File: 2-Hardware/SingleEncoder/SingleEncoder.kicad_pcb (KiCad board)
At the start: 2 copper layers, 20.3 x 57.2 mm, 26 parts, among them J1 PMOD_SINGLE, P1 CONN_01X06, Q1 MMBT2222, Q2 MMBT2222, U1 TPS60131, U2 MCP6L02, U3 ILD213T

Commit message: Finalized BOM
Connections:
- U3 pad 1: Net-(R3-Pad1) -> Net-(R4-Pad1)
- U3 pad 3: Net-(R4-Pad1) -> Net-(R3-Pad1)
- U3 pad 6: Net-(Q2-PadB) -> Net-(Q1-PadB)
- U3 pad 8: Net-(Q1-PadB) -> Net-(Q2-PadB)
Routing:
- net /ENC_A: track 0.13 -> 24.7 mm, vias 0 -> 2
- net GND: track 23.8 -> 41.8 mm, vias 5 -> 6
- net +5V: track 33.9 -> 51.8 mm, vias 0 -> 1
- net VCC: track 64.6 -> 67.8 mm
- net Net-(Q2-PadB): track 4.28 -> 7.20 mm
- net Net-(Q1-PadB): track 12.1 -> 9.22 mm
- net Net-(R4-Pad1): track 1.70 -> 2.72 mm
- net Net-(R3-Pad1): track 3.75 -> 2.72 mm
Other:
- net class Default: via_dia 0.6 -> 0.635; via_drill 0.4 -> 0.381
- board text added: "A"
- board text added: "B"
- board text added: "GND"
- board text added: "Quadrature Encoder PMOD-Compatible Interface"
- board text added: "Revision A Designed by: Ian McInerney"

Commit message: Added 4-pin connector behind the DIN connector
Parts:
- added P2: CONN_01X04, Connectors:CONN_2.54mm_1x4, F.Cu at (126.2, 107.6)
- moved D1 11.7 mm to (133.5, 95.9), turned to 180 degrees
- moved R2 9.56 mm to (133.5, 101.3), turned to 180 degrees
- moved C7 6.59 mm to (120.7, 101.3), turned to 0 degrees
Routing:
- net /ENC_A: track 24.7 -> 37.7 mm
- net /ENC_B: track 11.6 -> 20.3 mm
- net +5V: track 51.8 -> 54.0 mm
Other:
- board text added: "+5"

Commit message: Associated footprints, reimported to board. Layout not done.
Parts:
- removed Q1, Q2: MMBT2222, Transistors:TRANS_SOT-23-3_BEC
- removed R5, R6, R7, R8: 10k, SMD:SMD_0805
- removed U2: MCP6L02, SMD:SSOP_08_3.0mm_3.0mm_0.65mm
- removed U3: ILD213T, SMD:SOIC_08_4.0mm_5.8mm_1.27mm
- added AT1: TXB0102, SMD:SSOP_08_3.0mm_2.0mm_0.5mm, F.Cu at (151.1, 72.6)
- added C8: CAP, SMD:SMD_0805, F.Cu at (150.9, 79.1)
- added D2: PLVA653A, Diodes:DIODE_SOT-23-3, F.Cu at (157.4, 72.3)
- added D3: PLVA653A, Diodes:DIODE_SOT-23-3, F.Cu at (164.1, 72.3)
- C7: value 0.1uF -> CAP
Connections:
- net /PWR_EN renamed /EN
- C7 pad 1: GND -> VCC
- C7 pad 2: +5V -> GND
- R3 pad 2: Net-(R3-Pad2) -> /ENC_A
- R4 pad 2: Net-(R4-Pad2) -> /ENC_B
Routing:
- net (no net): track 0.00 -> 39.3 mm, vias 0 -> 4
- net GND: track 41.6 -> 25.6 mm, vias 6 -> 1
- net Net-(Q1-PadB): track 9.22 -> 0.00 mm
- net +5V: track 54.0 -> 45.6 mm
- net /ENC_A: track 37.7 -> 45.3 mm
- net Net-(R3-Pad2): track 7.60 -> 0.00 mm
- net Net-(Q2-PadB): track 7.20 -> 0.00 mm
- net /ENC_B: track 20.3 -> 27.5 mm
- net Net-(R4-Pad2): track 7.18 -> 0.00 mm
- net VCC: track 67.8 -> 69.4 mm, vias 1 -> 2

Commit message: Updated board layout to use level shifter
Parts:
- C7, C8: value CAP -> 0.1uF
- R1: moved to F.Cu
- moved D3 45.7 mm to (123.6, 93.3), turned to 90 degrees
- moved D2 35.4 mm to (128.9, 93.3), turned to 270 degrees
- moved C8 31.2 mm to (120.7, 86.7), turned to 180 degrees
- moved AT1 28.6 mm to (126.3, 86.7), turned to 90 degrees
- moved C7 18.6 mm to (132.0, 86.6)
- moved TP3 8.41 mm to (126.2, 79.4)
- moved R1 8.15 mm to (126.2, 82.8)
- moved R3 1.40 mm to (127.5, 99.1)
- moved R4 1.40 mm to (125.0, 99.1)
- moved TP1 1.27 mm to (133.9, 79.4)
- moved TP2 1.27 mm to (118.6, 79.4)
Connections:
- AT1 pad 2: Net-(AT1-Pad2) -> GND
- AT1 pad 3: Net-(AT1-Pad3) -> VCC
- AT1 pad 4: Net-(AT1-Pad4) -> /LOGIC_A
- AT1 pad 6: Net-(AT1-Pad6) -> /EN
- AT1 pad 7: Net-(AT1-Pad7) -> +5V
- D2 pad C: Net-(D2-PadC) -> Net-(AT1-Pad1)
- J1 pad 2: /LOGIC_B -> Net-(J1-Pad2)
- J1 pad 4: Net-(J1-Pad4) -> /LOGIC_B
- R3 pad 1: Net-(D2-PadC) -> Net-(AT1-Pad1)
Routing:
- net (no net): track 39.3 -> 0.00 mm, vias 4 -> 0
- net /ENC_A: track 45.3 -> 19.6 mm, vias 2 -> 0
- net /ENC_B: track 27.5 -> 14.1 mm
- net Net-(AT1-Pad1): track 0.00 -> 10.9 mm
- net Net-(AT1-Pad8): track 2.72 -> 10.8 mm
- net GND: track 25.6 -> 17.9 mm, vias 1 -> 5
- net +5V: track 45.6 -> 52.5 mm, vias 1 -> 2
- net /EN: track 44.5 -> 38.1 mm
- net VCC: track 69.4 -> 64.4 mm, vias 2 -> 1
- net /LOGIC_A: track 12.6 -> 16.0 mm
- net Net-(D2-PadC): track 2.72 -> 0.00 mm
- net /LOGIC_B: track 18.8 -> 20.9 mm
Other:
- net class EN added: clearance 0.2, trace_width 0.1524, via_dia 0.635, via_drill 0.381
- rule trace_min: 0.2 -> 0.1524
- board text added: "Revision B Designed by: Ian McInerney"
- board text removed: "Revision A Designed by: Ian McInerney"

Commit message: Updated PMOD connector holes
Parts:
- J1: footprint Connectors:PMOD_SINGLE_MALE -> Digilent:PMOD_SINGLE_MALE
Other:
- rule pad_to_mask_clearance: 0 -> 0.0762
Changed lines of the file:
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@@
     (links 60)
     (no_connects 0)
-    (area 116.027999 68.656999 136.448001 125.907001)
+    (area 114.179905 68.431999 138.296096 127.765)
     (thickness 1.6)
     (drawings 13)
@@
     (pad_size 3.38 2.4)
     (pad_drill 0)
-    (pad_to_mask_clearance 0)
+    (pad_to_mask_clearance 0.0762)
+    (solder_mask_min_width 0.1016)
     (aux_axis_origin 0 0)
     (visible_elements FFFFFF7F)
@@
     )
   )
-  (module Connectors:PMOD_SINGLE_MALE locked (layer F.Cu)
-    (at 126.238 70.485)
-    (fp_text reference J1 (at 5.588 4.318) (layer F.SilkS)
-      (effects (font (size 1 1) (thickness 0.15)))
-    )
-    (fp_text value PMOD_SINGLE (at 0 0) (layer F.Fab) hide
-      (effects (font (size 1 1) (thickness 0.15)))
-    )
-    (fp_line (start -10.16 -1.778) (end 10.16 -1.778) (layer Dwgs.User) (width 0.15))
-    (fp_line (start 5.08 0.762) (end 5.08 3.302) (layer F.SilkS) (width 0.15))
-    (fp_line (start 7.62 0.762) (end 7.62 3.302) (layer F.SilkS) (width 0.15))
-    (fp_line (start 7.62 3.302) (end -7.62 3.302) (layer F.SilkS) (width 0.15))
-    (fp_line (start -7.62 3.302) (end -7.62 0.762) (layer F.SilkS) (width 0.15))
-    (fp_line (start -7.62 0.762) (end 7.62 0.762) (layer F.SilkS) (width 0.15))
-    (pad 1 thru_hole rect (at 6.35 2.032 180) (size 1.524 1.524) (drill 0.762) (layers *.Cu *.Mask F.SilkS)
-      (net 7 /LOGIC_A))
-    (pad 2 thru_hole circle (at 3.81 2.032 180) (size 1.524 1.524) (drill 0.762) (layers *.Cu *.Mask F.SilkS)
-      (net 19 "Net-(J1-Pad2)"))
-    (pad 3 thru_hole circle (at 1.27 2.032 180) (size 1.524 1.524) (drill 0.762) (layers *.Cu *.Mask F.SilkS)
-      (net 16 /EN))
-    (pad 4 thru_hole circle (at -1.27 2.032 180) (size 1.524 1.524) (drill 0.762) (layers *.Cu *.Mask F.SilkS)
-      (net 8 /LOGIC_B))
-    (pad 5 thru_hole circle (at -3.81 2.032 180) (size 1.524 1.524) (drill 0.762) (layers *.Cu *.Mask F.SilkS)
-      (net 2 GND))
-    (pad 6 thru_hole circle (at -6.35 2.032 180) (size 1.524 1.524) (drill 0.762) (layers *.Cu *.Mask F.SilkS)
-      (net 1 VCC))
-    (model 3D/Connectors/CONN_1x6_Male.wrl
-      (at (xyz -0.3 0.31 0.096))
-      (scale (xyz 0.3937 0.3937 0.3937))
-      (rotate (xyz 0 180 180))
-    )
-  )
   (module SMD:SMD_0805 (layer F.Cu)
     (at 126.238 82.804 270)
@@
       (scale (xyz 0.3937 0.3937 0.3937))
       (rotate (xyz 0 0 90))
+    )
+  )
+  (module Digilent:PMOD_SINGLE_MALE locked (layer F.Cu)
+    (at 126.238 70.485)
+    (fp_text reference J1 (at 5.588 4.318) (layer F.SilkS)
+      (effects (font (size 1 1) (thickness 0.15)))
+    )
+    (fp_text value PMOD_SINGLE (at 0 0) (layer F.Fab) hide
+      (effects (font (size 1 1) (thickness 0.15)))
+    )
+    (fp_line (start -10.16 -1.778) (end 10.16 -1.778) (layer Dwgs.User) (width 0.15))
+    (fp_line (start 5.08 0.762) (end 5.08 3.302) (layer F.SilkS) (width 0.15))
+    (fp_line (start 7.62 0.762) (end 7.62 3.302) (layer F.SilkS) (width 0.15))
+    (fp_line (start 7.62 3.302) (end -7.62 3.302) (layer F.SilkS) (width 0.15))
+    (fp_line (start -7.62 3.302) (end -7.62 0.762) (layer F.SilkS) (width 0.15))
+    (fp_line (start -7.62 0.762) (end 7.62 0.762) (layer F.SilkS) (width 0.15))
+    (pad 1 thru_hole rect (at 6.35 2.032 180) (size 1.7018 1.7018) (drill 0.9906) (layers *.Cu *.Mask F.SilkS)
+      (net 7 /LOGIC_A))
+    (pad 2 thru_hole circle (at 3.81 2.032 180) (size 1.778 1.778) (drill 0.9906) (layers *.Cu *.Mask F.SilkS)
+      (net 19 "Net-(J1-Pad2)"))
+    (pad 3 thru_hole circle (at 1.27 2.032 180) (size 1.778 1.778) (drill 0.9906) (layers *.Cu *.Mask F.SilkS)
+      (net 16 /EN))
+    (pad 4 thru_hole circle (at -1.27 2.032 180) (size 1.778 1.778) (drill 0.9906) (layers *.Cu *.Mask F.SilkS)
+      (net 8 /LOGIC_B))
+    (pad 5 thru_hole circle (at -3.81 2.032 180) (size 1.778 1.778) (drill 0.9906) (layers *.Cu *.Mask F.SilkS)
+      (net 2 GND))
+    (pad 6 thru_hole circle (at -6.35 2.032 180) (size 1.778 1.778) (drill 0.9906) (layers *.Cu *.Mask F.SilkS)
+      (net 1 VCC))
+    (model 3D/Connectors/CONN_1x6_Male.wrl
+      (at (xyz -0.3 0.31 0.096))
+      (scale (xyz 0.3937 0.3937 0.3937))
+      (rotate (xyz 0 180 180))
     )
   )
@@
   (segment (start 129.0265 85.991) (end 129.0265 84.2065) (width 0.25) (layer F.Cu) (net 7))
   (segment (start 129.0265 84.2065) (end 133.858 79.375) (width 0.25) (layer F.Cu) (net 7))
-  (segment (start 118.618 79.375) (end 122.4915 79.375) (width 0.25) (layer F.Cu) (net 8) (status 400000))
-  (segment (start 123.698 73.787) (end 124.968 72.517) (width 0.25) (layer F.Cu) (net 8) (status 800000))
+  (segment (start 118.618 79.375) (end 122.4915 79.375) (width 0.25) (layer F.Cu) (net 8))
+  (segment (start 123.698 73.787) (end 124.968 72.517) (width 0.25) (layer F.Cu) (net 8))
   (segment (start 123.698 78.1685) (end 123.698 73.787) (width 0.25) (layer F.Cu) (net 8))
   (segment (start 122.4915 79.375) (end 123.698 78.1685) (width 0.25) (layer F.Cu) (net 8))

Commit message: Updated isolation circuit
- Swapped TXB0102 for 2 TXB0101
- Re-did board layout to accomodate new parts
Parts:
- added AT2: TXB0101, SMD:SOT-23-6, F.Cu at (121.9, 86.2)
- added C10: 0.1uF, SMD:SMD_0805, F.Cu at (118.7, 86.2)
- added C9: 0.1uF, SMD:SMD_0805, F.Cu at (125.2, 86.3)
- AT1: value TXB0102 -> TXB0101; footprint SMD:SSOP_08_3.0mm_2.0mm_0.5mm -> SMD:SOT-23-6
- moved C8 6.68 mm to (127.3, 86.3), turned to 0 degrees
- moved AT1 4.28 mm to (130.6, 86.2)
- moved C7 2.01 mm to (133.9, 86.2)
- moved R1 0.13 mm to (126.2, 82.7)
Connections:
- AT1 pad 1: Net-(AT1-Pad1) -> VCC
- AT1 pad 3: VCC -> Net-(AT1-Pad3)
- AT1 pad 5: /LOGIC_B -> /EN
- AT1 pad 6: /EN -> +5V
- C7 pad 1: VCC -> +5V
- C8 pad 1: +5V -> VCC
- D2 pad C: Net-(AT1-Pad1) -> Net-(AT1-Pad3)
- D3 pad C: Net-(AT1-Pad8) -> Net-(AT2-Pad3)
- R3 pad 1: Net-(AT1-Pad1) -> Net-(AT1-Pad3)
- R4 pad 1: Net-(AT1-Pad8) -> Net-(AT2-Pad3)
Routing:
- net GND: track 17.9 -> 36.5 mm
- net Net-(AT2-Pad3): track 0.00 -> 13.6 mm
- net Net-(AT1-Pad3): track 0.00 -> 11.3 mm
- net Net-(AT1-Pad1): track 10.9 -> 0.00 mm
- net Net-(AT1-Pad8): track 10.8 -> 0.00 mm
- net /EN: track 38.1 -> 47.6 mm, vias 1 -> 3
- net /LOGIC_A: track 16.0 -> 18.8 mm
- net +5V: track 52.5 -> 55.0 mm
- net VCC: track 64.4 -> 62.3 mm, vias 1 -> 3
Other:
- board text added: "Revision C Designed by: Ian McInerney"
- board text removed: "Revision B Designed by: Ian McInerney"

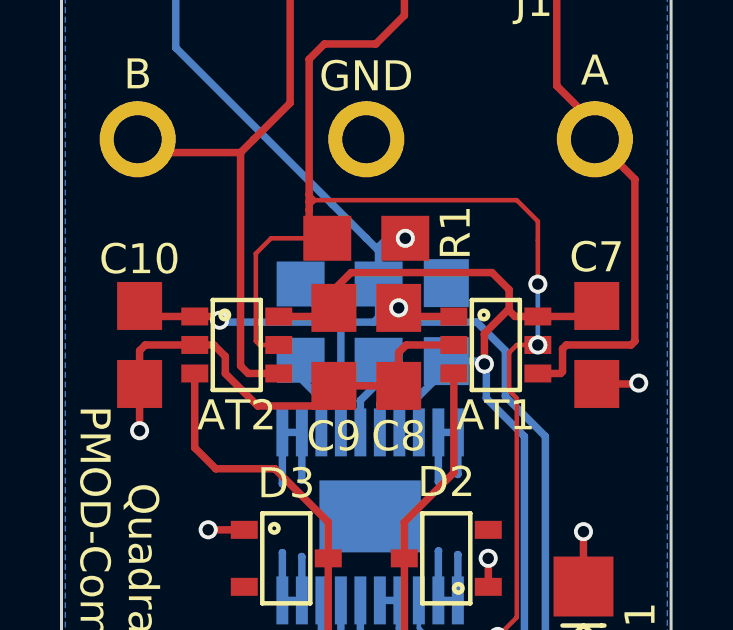
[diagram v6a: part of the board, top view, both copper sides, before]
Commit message: Revised layout and created BOM
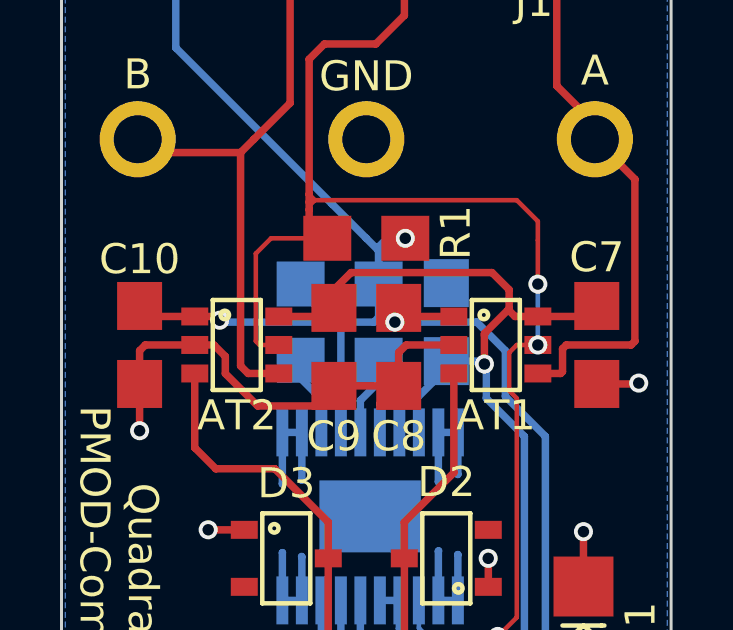
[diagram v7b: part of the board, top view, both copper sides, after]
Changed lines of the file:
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@@
   (gr_line (start 136.398 68.707) (end 116.078 68.707) (angle 90) (layer Edge.Cuts) (width 0.1))
   (gr_line (start 116.078 125.857) (end 136.398 125.857) (angle 90) (layer Edge.Cuts) (width 0.1))
+  (via (at 127.1905 85.471) (size 0.635) (drill 0.381) (layers F.Cu B.Cu) (net 1) (status 800000))
+  (segment (start 127.1905 85.471) (end 127.3175 85.344) (width 0.25) (layer F.Cu) (net 1) (status C00000))
+  (segment (start 127.3175 85.344) (end 127.3175 84.9965) (width 0.25) (layer F.Cu) (net 1) (status C00000))
   (segment (start 125.603 85.471) (end 121.412 85.471) (width 0.25) (layer B.Cu) (net 1))
   (segment (start 121.224 85.283) (end 120.52 85.283) (width 0.25) (layer F.Cu) (net 1))
@@
   (segment (start 126.9365 82.677) (end 126.649 82.9645) (width 0.25) (layer B.Cu) (net 1))
   (segment (start 127.538 82.677) (end 126.9365 82.677) (width 0.25) (layer B.Cu) (net 1))
-  (via (at 127.3175 84.9965) (size 0.635) (drill 0.381) (layers F.Cu B.Cu) (net 1))
-  (segment (start 127.3175 84.9965) (end 127.3175 85.471) (width 0.25) (layer B.Cu) (net 1))
-  (segment (start 127.3175 85.471) (end 127.3175 85.4075) (width 0.25) (layer B.Cu) (net 1))
-  (segment (start 127.3175 85.4075) (end 127.3175 85.471) (width 0.25) (layer B.Cu) (net 1))
   (segment (start 131.699 98.552) (end 131.7625 98.552) (width 0.25) (layer B.Cu) (net 1))
   (segment (start 131.7625 98.552) (end 132.207 98.1075) (width 0.25) (layer B.Cu) (net 1))
@@
   (segment (start 131.699 98.552) (end 130.302 98.552) (width 0.25) (layer B.Cu) (net 1))
   (segment (start 126.873 85.471) (end 126.649 85.247) (width 0.25) (layer B.Cu) (net 1))
-  (segment (start 127.3175 85.471) (end 126.873 85.471) (width 0.25) (layer B.Cu) (net 1))
+  (segment (start 127.3175 85.471) (end 127.1905 85.471) (width 0.25) (layer B.Cu) (net 1))
+  (segment (start 127.1905 85.471) (end 126.873 85.471) (width 0.25) (layer B.Cu) (net 1))
   (segment (start 127.538 84.776) (end 127.3175 84.9965) (width 0.25) (layer F.Cu) (net 1))
   (segment (start 129.156 85.283) (end 127.604 85.283) (width 0.25) (layer F.Cu) (net 1))
